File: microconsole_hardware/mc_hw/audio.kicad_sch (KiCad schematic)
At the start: 47 parts, among them U5 PCM5102APWR, U6 PAM8302AADCR, U7 PAM8406DR

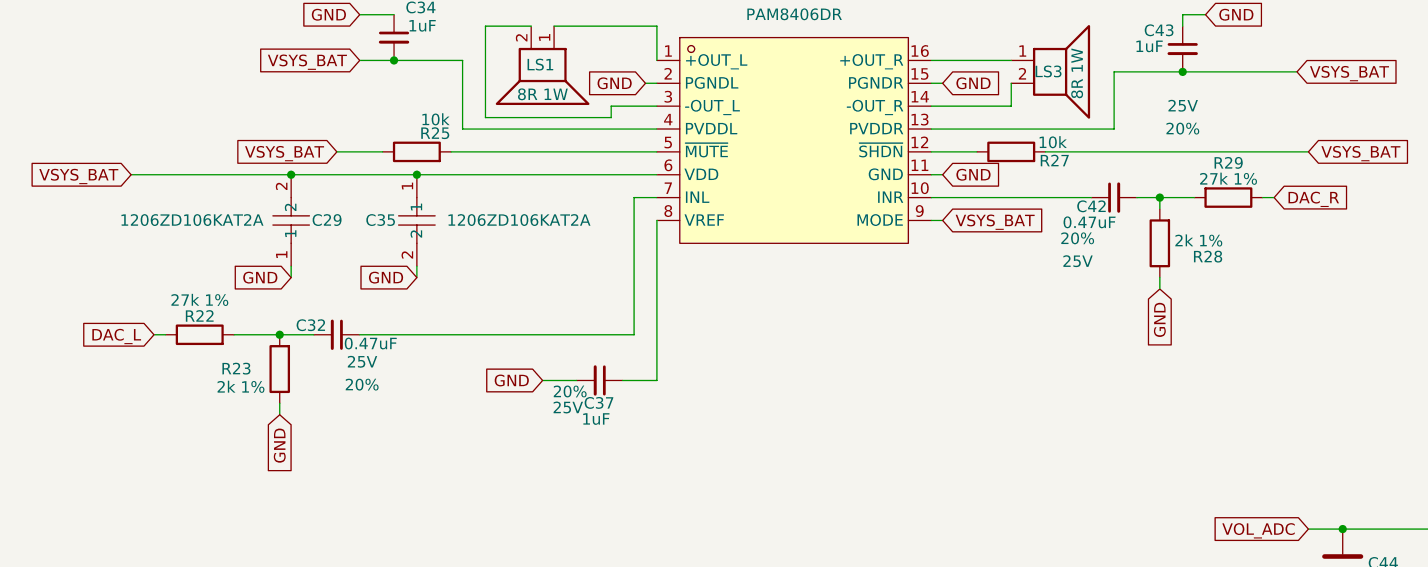
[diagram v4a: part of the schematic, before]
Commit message: cleanup caps and resistors
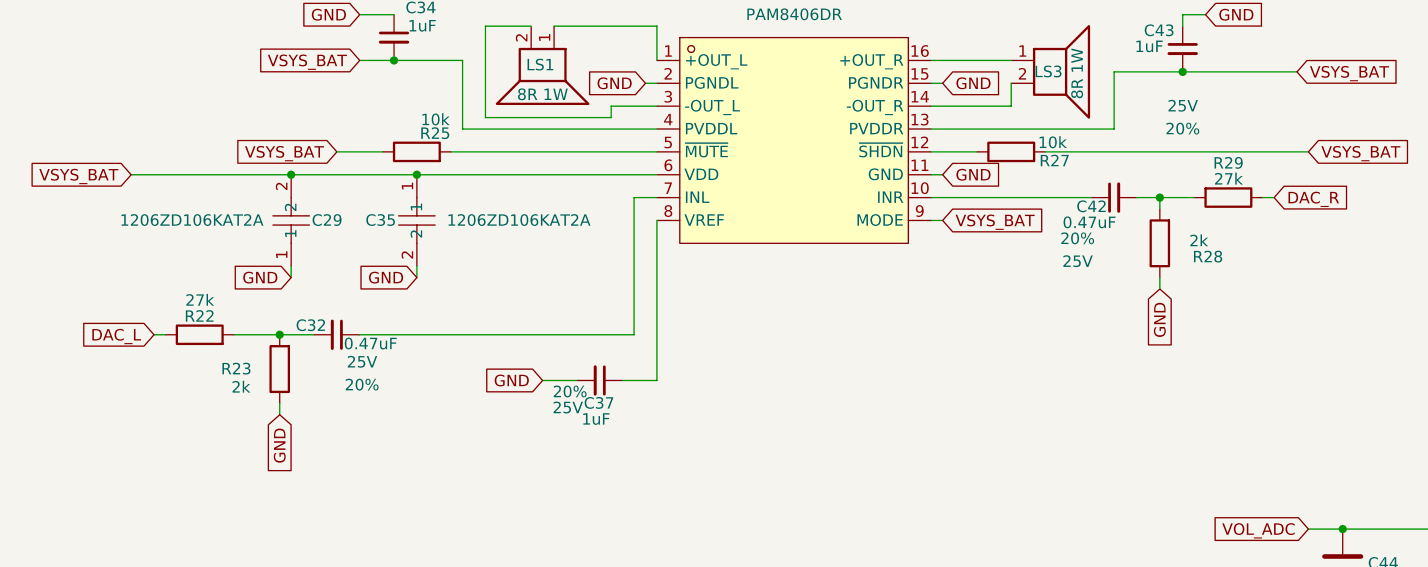
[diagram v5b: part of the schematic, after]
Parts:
- C18, C19, C22, C23, C28, C30, C31, C32, C34, C37, C39, C42, C43: footprint PCM_SparkFun-Capacitor:C_0805_2012Metric -> Capacitor_SMD:C_0805_2012Metric
- R22, R29: value 27k 1% -> 27k
- R23, R28: value 2k 1% -> 2k
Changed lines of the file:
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@@
 			)
 		)
-		(property "Footprint" "PCM_SparkFun-Capacitor:C_0805_2012Metric"
+		(property "Footprint" "Capacitor_SMD:C_0805_2012Metric"
 			(at 52.07 59.69 0)
 			(hide yes)
@@
 			)
 		)
-		(property "Footprint" "PCM_SparkFun-Capacitor:C_0805_2012Metric"
+		(property "Footprint" "Capacitor_SMD:C_0805_2012Metric"
 			(at 196.85 107.95 0)
 			(hide yes)
@@
 			)
 		)
-		(property "Footprint" "PCM_SparkFun-Capacitor:C_0805_2012Metric"
+		(property "Footprint" "Capacitor_SMD:C_0805_2012Metric"
 			(at 81.28 53.34 0)
 			(hide yes)
@@
 			)
 		)
-		(property "Value" "2k 1%"
+		(property "Value" "2k"
 			(at 194.818 112.776 0)
 			(show_name no)
@@
 			)
 		)
-		(property "Footprint" "PCM_SparkFun-Capacitor:C_0805_2012Metric"
+		(property "Footprint" "Capacitor_SMD:C_0805_2012Metric"
 			(at 87.63 123.19 0)
 			(hide yes)
@@
 			)
 		)
-		(property "Footprint" "PCM_SparkFun-Capacitor:C_0805_2012Metric"
+		(property "Footprint" "Capacitor_SMD:C_0805_2012Metric"
 			(at 107.95 175.26 0)
 			(hide yes)
@@
 			)
 		)
-		(property "Value" "27k 1%"
+		(property "Value" "27k"
 			(at 83.82 119.38 90)
 			(show_name no)
@@
 			)
 		)
-		(property "Footprint" "PCM_SparkFun-Capacitor:C_0805_2012Metric"
+		(property "Footprint" "Capacitor_SMD:C_0805_2012Metric"
 			(at 149.86 190.5 0)
 			(hide yes)
@@
 			)
 		)
-		(property "Footprint" "PCM_SparkFun-Capacitor:C_0805_2012Metric"
+		(property "Footprint" "Capacitor_SMD:C_0805_2012Metric"
 			(at 52.07 69.85 0)
 			(hide yes)
@@
 			)
 		)
-		(property "Footprint" "PCM_SparkFun-Capacitor:C_0805_2012Metric"
+		(property "Footprint" "Capacitor_SMD:C_0805_2012Metric"
 			(at 59.69 185.42 0)
 			(hide yes)
@@
 			)
 		)
-		(property "Footprint" "PCM_SparkFun-Capacitor:C_0805_2012Metric"
+		(property "Footprint" "Capacitor_SMD:C_0805_2012Metric"
 			(at 193.04 102.87 0)
 			(hide yes)
@@
 			)
 		)
-		(property "Value" "2k 1%"
+		(property "Value" "2k"
 			(at 88.392 129.032 0)
 			(show_name no)
@@
 			)
 		)
-		(property "Footprint" "PCM_SparkFun-Capacitor:C_0805_2012Metric"
+		(property "Footprint" "Capacitor_SMD:C_0805_2012Metric"
 			(at 105.41 101.6 0)
 			(hide yes)
@@
 			)
 		)
-		(property "Footprint" "PCM_SparkFun-Capacitor:C_0805_2012Metric"
+		(property "Footprint" "Capacitor_SMD:C_0805_2012Metric"
 			(at 116.84 128.27 0)
 			(hide yes)
@@
 			)
 		)
-		(property "Value" "27k 1%"
+		(property "Value" "27k"
 			(at 198.12 105.918 90)
 			(show_name no)
@@
 			)
 		)
-		(property "Footprint" "PCM_SparkFun-Capacitor:C_0805_2012Metric"
+		(property "Footprint" "Capacitor_SMD:C_0805_2012Metric"
 			(at 85.09 182.88 0)
 			(hide yes)
@@
 			)
 		)
-		(property "Footprint" "PCM_SparkFun-Capacitor:C_0805_2012Metric"
+		(property "Footprint" "Capacitor_SMD:C_0805_2012Metric"
 			(at 55.88 34.29 0)
 			(hide yes)

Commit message: fix capacitors
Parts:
- removed C30: 0.22uF, Capacitor_SMD:C_0805_2012Metric, symbol PCM_SparkFun-Capacitor:2.2uF_0805_25V_20%
- removed C42: 0.47uF, Capacitor_SMD:C_0805_2012Metric, symbol PCM_SparkFun-Capacitor:2.2uF_0805_25V_20%
- removed C43: 1uF, Capacitor_SMD:C_0805_2012Metric, symbol PCM_SparkFun-Capacitor:2.2uF_0805_25V_20%
- added C59: 0.22uF, Capacitor_SMD:C_0805_2012Metric, symbol Device:C
- added C72: 0.47uF, Capacitor_SMD:C_0805_2012Metric, symbol Device:C
- added C73: 1uF, Capacitor_SMD:C_0805_2012Metric, symbol Device:C
- C18, C19, C22, C23, C28, C31, C32, C34, C37, C39: symbol PCM_SparkFun-Capacitor:2.2uF_0805_25V_20% -> Device:C
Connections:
- net CENTER_FEED: now also C59.1
- net GND: now also C73.1
- net VSYS_BAT: now also C73.2
- net at U7.10 (INR): now also C72.1
- net at R28.2, R29.2: now also C72.2
- net at U6.3 (IN+): now also C59.2
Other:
- moved on the sheet: C19, C23, C28, C31, C32, C34, C37, R18

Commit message: cleanup ic symbol pin types
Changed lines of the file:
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@@
 	)
 	(junction
-		(at 144.78 175.26)
-		(diameter 0)
-		(color 0 0 0 0)
-	)
-	(junction
 		(at 107.95 166.37)
 		(diameter 0)
@@
 	)
 	(junction
-		(at 165.1 107.95)
-		(diameter 0)
-		(color 0 0 0 0)
-	)
-	(junction
 		(at 210.82 144.78)
 		(diameter 0)
@@
 	)
 	(junction
+		(at 73.66 27.94)
+		(diameter 0)
+		(color 0 0 0 0)
+	)
+	(junction
 		(at 34.29 66.04)
 		(diameter 0)
@@
 	(wire
 		(pts
+			(xy 73.66 27.94) (xy 91.44 27.94)
+		)
+		(stroke
+			(width 0)
+			(type default)
+		)
+	)
+	(wire
+		(pts
 			(xy 97.79 166.37) (xy 100.33 166.37)
 		)
@@
 	(wire
 		(pts
-			(xy 144.78 175.26) (xy 144.78 176.53)
-		)
-		(stroke
-			(width 0)
-			(type default)
-		)
-	)
-	(wire
-		(pts
 			(xy 116.84 39.37) (xy 132.08 39.37)
 		)
@@
 	(wire
 		(pts
-			(xy 29.21 27.94) (xy 91.44 27.94)
+			(xy 29.21 27.94) (xy 73.66 27.94)
 		)
 		(stroke
@@
 	(wire
 		(pts
-			(xy 144.78 175.26) (xy 149.86 175.26)
-		)
-		(stroke
-			(width 0)
-			(type default)
-		)
-	)
-	(wire
-		(pts
 			(xy 31.75 170.18) (xy 33.02 170.18)
 		)
@@
 	(wire
 		(pts
-			(xy 135.89 175.26) (xy 144.78 175.26)
+			(xy 135.89 175.26) (xy 149.86 175.26)
 		)
 		(stroke
@@
 	(wire
 		(pts
-			(xy 162.56 107.95) (xy 165.1 107.95)
-		)
-		(stroke
-			(width 0)
-			(type default)
-		)
-	)
-	(wire
-		(pts
 			(xy 168.91 46.99) (xy 168.91 49.53)
 		)
@@
 					(unit 1)
 				)
+			)
+		)
+	)
+	(symbol
+		(lib_id "power:PWR_FLAG")
+		(at 73.66 27.94 0)
+		(unit 1)
+		(body_style 1)
+		(exclude_from_sim no)
+		(in_bom yes)
+		(on_board yes)
+		(in_pos_files yes)
+		(dnp no)
+		(fields_autoplaced yes)
+		(property "Reference" "#FLG03"
+			(at 73.66 26.035 0)
+			(hide yes)
+			(show_name no)
+			(do_not_autoplace no)
+			(effects
+				(font
+					(size 1.27 1.27)
+				)
+			)
+		)
+		(property "Value" "PWR_FLAG"
+			(at 73.66 22.86 0)
+			(show_name no)
+			(do_not_autoplace no)
+			(effects
+				(font
+					(size 1.27 1.27)
+				)
+			)
+		)
+		(property "Footprint" ""
+			(at 73.66 27.94 0)
+			(hide yes)
+			(show_name no)
+			(do_not_autoplace no)
+			(effects
+				(font
+					(size 1.27 1.27)
+				)
+			)
+		)
+		(property "Datasheet" ""
+			(at 73.66 27.94 0)
+			(hide yes)
+			(show_name no)
+			(do_not_autoplace no)
+			(effects
+				(font
+					(size 1.27 1.27)
+				)
+			)
+		)
+		(property "Description" "Special symbol for telling ERC where power comes from"
+			(at 73.66 27.94 0)
+			(hide yes)
+			(show_name no)
+			(do_not_autoplace no)
+			(effects
+				(font
+					(size 1.27 1.27)
+				)
+			)
+		)
+		(pin "1"
+		)
+		(instances
+			(project "top"
+				(path "/3433afdc-e53a-48bd-a2b1-9fdee73e8b40/1a1f5339-d8f7-4e0d-9eaf-95ca89a6e02d"
+					(reference "#FLG03")
+					(unit 1)
+				)

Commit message: consolidate parts 1
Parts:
- R16, R17, R25, R26, R27: MPN (none) -> RC0603FR-0710KL; Manufacturer (none) -> YAGEO; Power (none) -> 0.1W; Tolerance (none) -> 1%
- R18, R19: MPN (none) -> RC0603FR-07470RL; Manufacturer (none) -> YAGEO; Power (none) -> 0.1W; Tolerance (none) -> 1%
- R20: MPN (none) -> RC0603FR-0733KL; Manufacturer (none) -> YAGEO; Power (none) -> 0.1W; Tolerance (none) -> 1%
- R21: MPN (none) -> RC0603FR-074K7L; Manufacturer (none) -> YAGEO; Power (none) -> 0.1W; Tolerance (none) -> 1%
- R22, R29: MPN (none) -> RC0603FR-0727KL; Manufacturer (none) -> YAGEO; Power (none) -> 0.1W; Tolerance (none) -> 1%
- R23, R28: MPN (none) -> RC0603FR-072KL; Manufacturer (none) -> YAGEO; Power (none) -> 0.1W; Tolerance (none) -> 1%
- R24: MPN (none) -> RC0603FR-07100KL; Manufacturer (none) -> YAGEO; Power (none) -> 0.1W; Tolerance (none) -> 1%
- RV1: Power (none) -> 0.1W; Tolerance (none) -> 1%
